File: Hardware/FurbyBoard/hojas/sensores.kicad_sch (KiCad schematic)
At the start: 39 parts, among them J10 Luz ×2, altavoz ×2, J7 IR: emisor ×2, receptor ×3, G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, J8 Inclinación ×3, lengua ×2, J9 Leva ×2, encoder ×4, barriga 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, Q2 AO3400A, Q3 AO3400A, U10 TCA9535PWR, U11 SN74LVC1G17DBVR

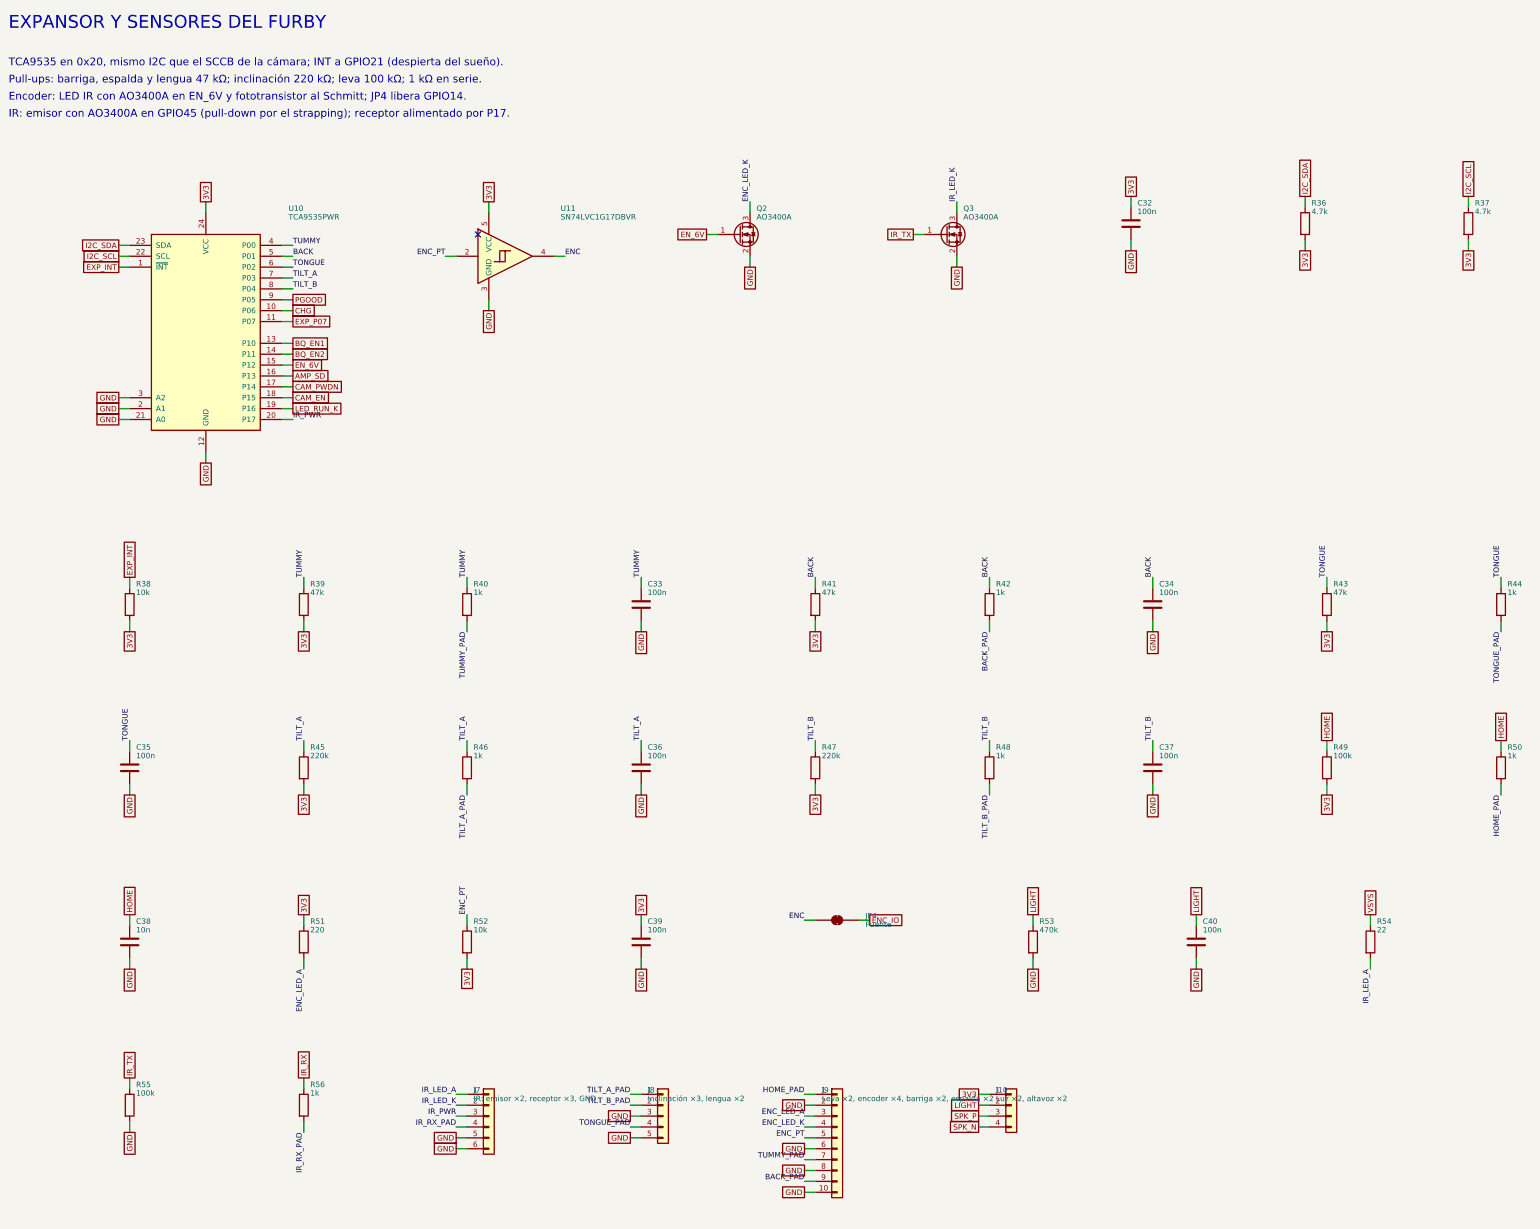
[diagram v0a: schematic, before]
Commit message: Refactor: pads de cable agrupados por zona y etiquetas globales
- Motor en J9 con leva, encoder y sensores; altavoz en J8 con inclinación y
  lengua; luz en J7 con el IR. Desaparecen J4 y J10: cada grupo sale por el
  borde más cercano a su destino.
- Micro en 2x03 en vez de 1x06 para que quepa junto al borde derecho.
- Todas las etiquetas del esquemático son globales, así el nombre de red
  coincide con el del PCB (paridad sin prefijos de hoja).
- ERC 0 errores, 0 avisos.

Co-Authored-By: Claude Opus 5.5 (1M context) <noreply@anthropic.com>
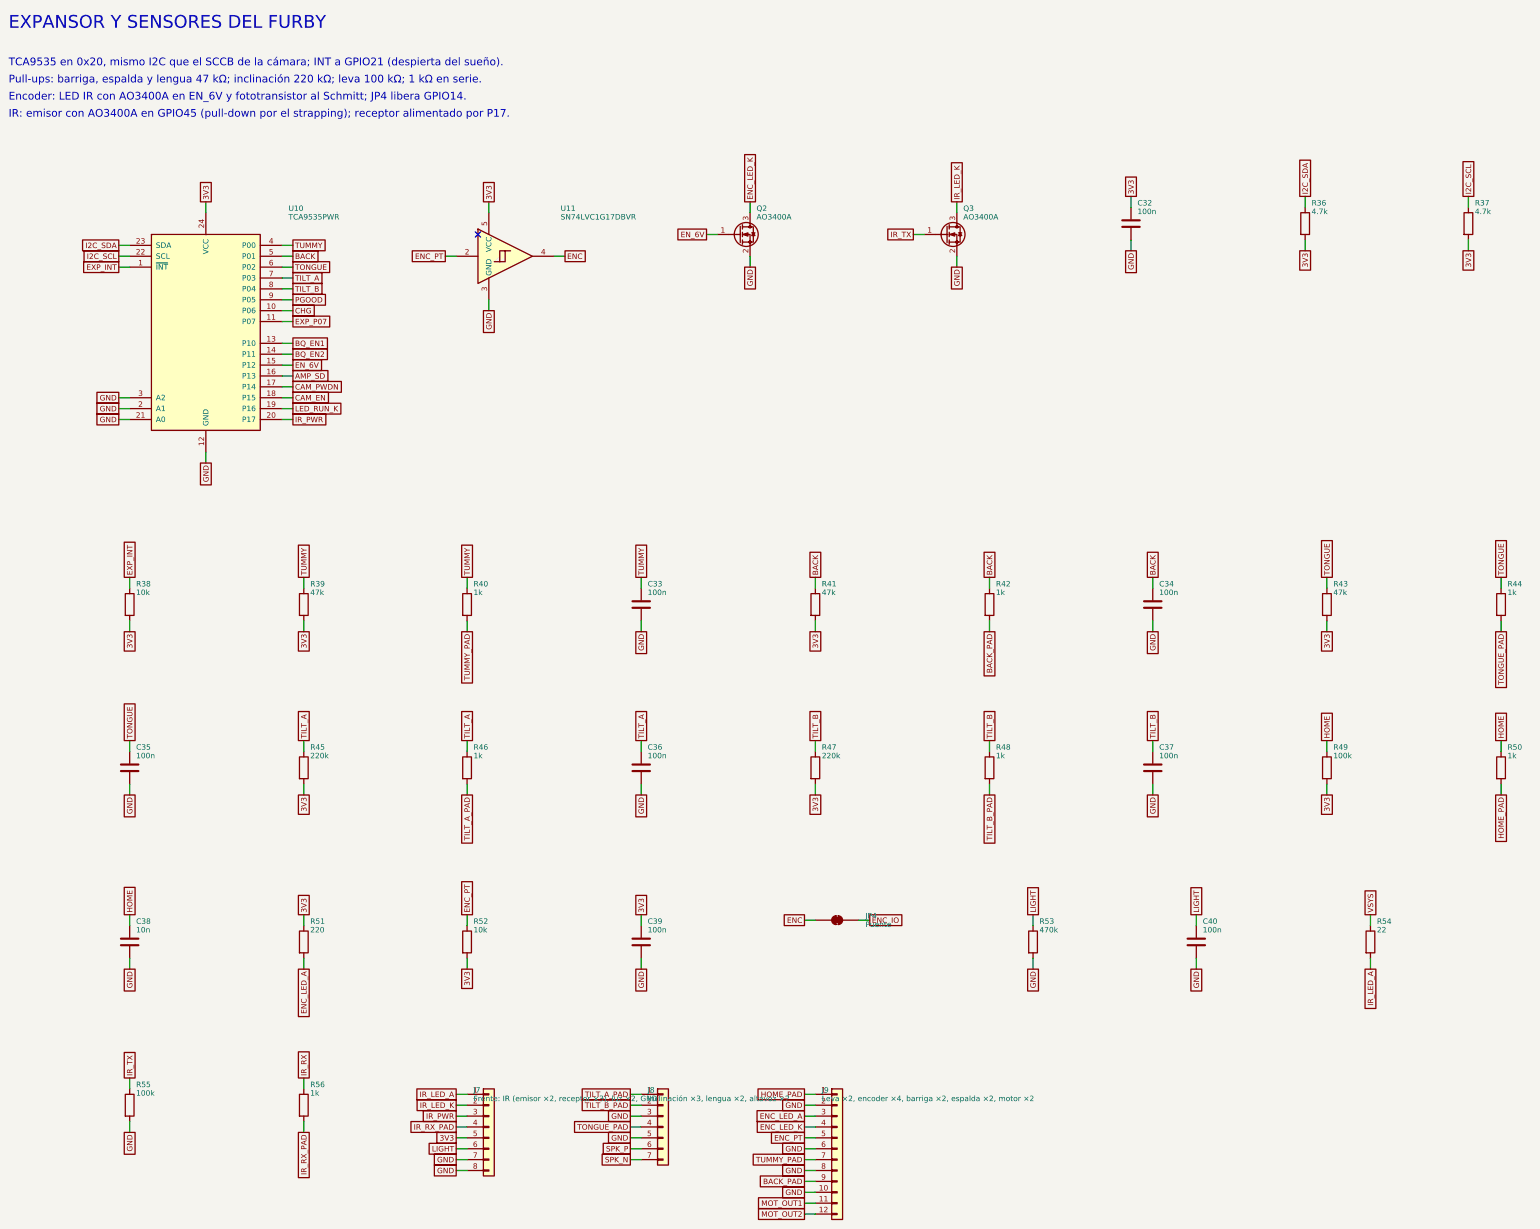
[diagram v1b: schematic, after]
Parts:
- removed J10: Luz ×2, altavoz ×2, FurbyBoard:Pads_2x02_P2.54mm, symbol Connector_Generic:Conn_01x04
- J7: value IR: emisor ×2, receptor ×3, GND -> Frente: IR (emisor ×2, receptor ×3), luz ×2, GND; footprint FurbyBoard:Pads_2x03_P2.54mm -> FurbyBoard:Pads_2x04_P2.54mm; symbol Connector_Generic:Conn_01x06 -> Connector_Generic:Conn_01x08
- J8: value Inclinación ×3, lengua ×2 -> Inclinación ×3, lengua ×2, altavoz ×2; footprint FurbyBoard:Pads_1x05_P2.54mm -> FurbyBoard:Pads_1x07_P2.54mm; symbol Connector_Generic:Conn_01x05 -> Connector_Generic:Conn_01x07
- J9: value Leva ×2, encoder ×4, barriga ×2, espalda ×2 -> Leva ×2, encoder ×4, barriga ×2, espalda ×2, motor ×2; footprint FurbyBoard:Pads_2x05_P2.54mm -> FurbyBoard:Pads_2x06_P2.54mm; symbol Connector_Generic:Conn_01x10 -> Connector_Generic:Conn_01x12
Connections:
- net 3V3: now also J7.5 (Pin_5)
- net GND: now also J7.7 (Pin_7), J7.8 (Pin_8); no longer J7.5 (Pin_5), J7.6 (Pin_6)
- net LIGHT: now also J7.6 (Pin_6)
- net SPK_N: now also J8.7 (Pin_7)
- net SPK_P: now also J8.6 (Pin_6)
- new net MOT_OUT1: J9.11 (Pin_11)
- new net MOT_OUT2: J9.12 (Pin_12)

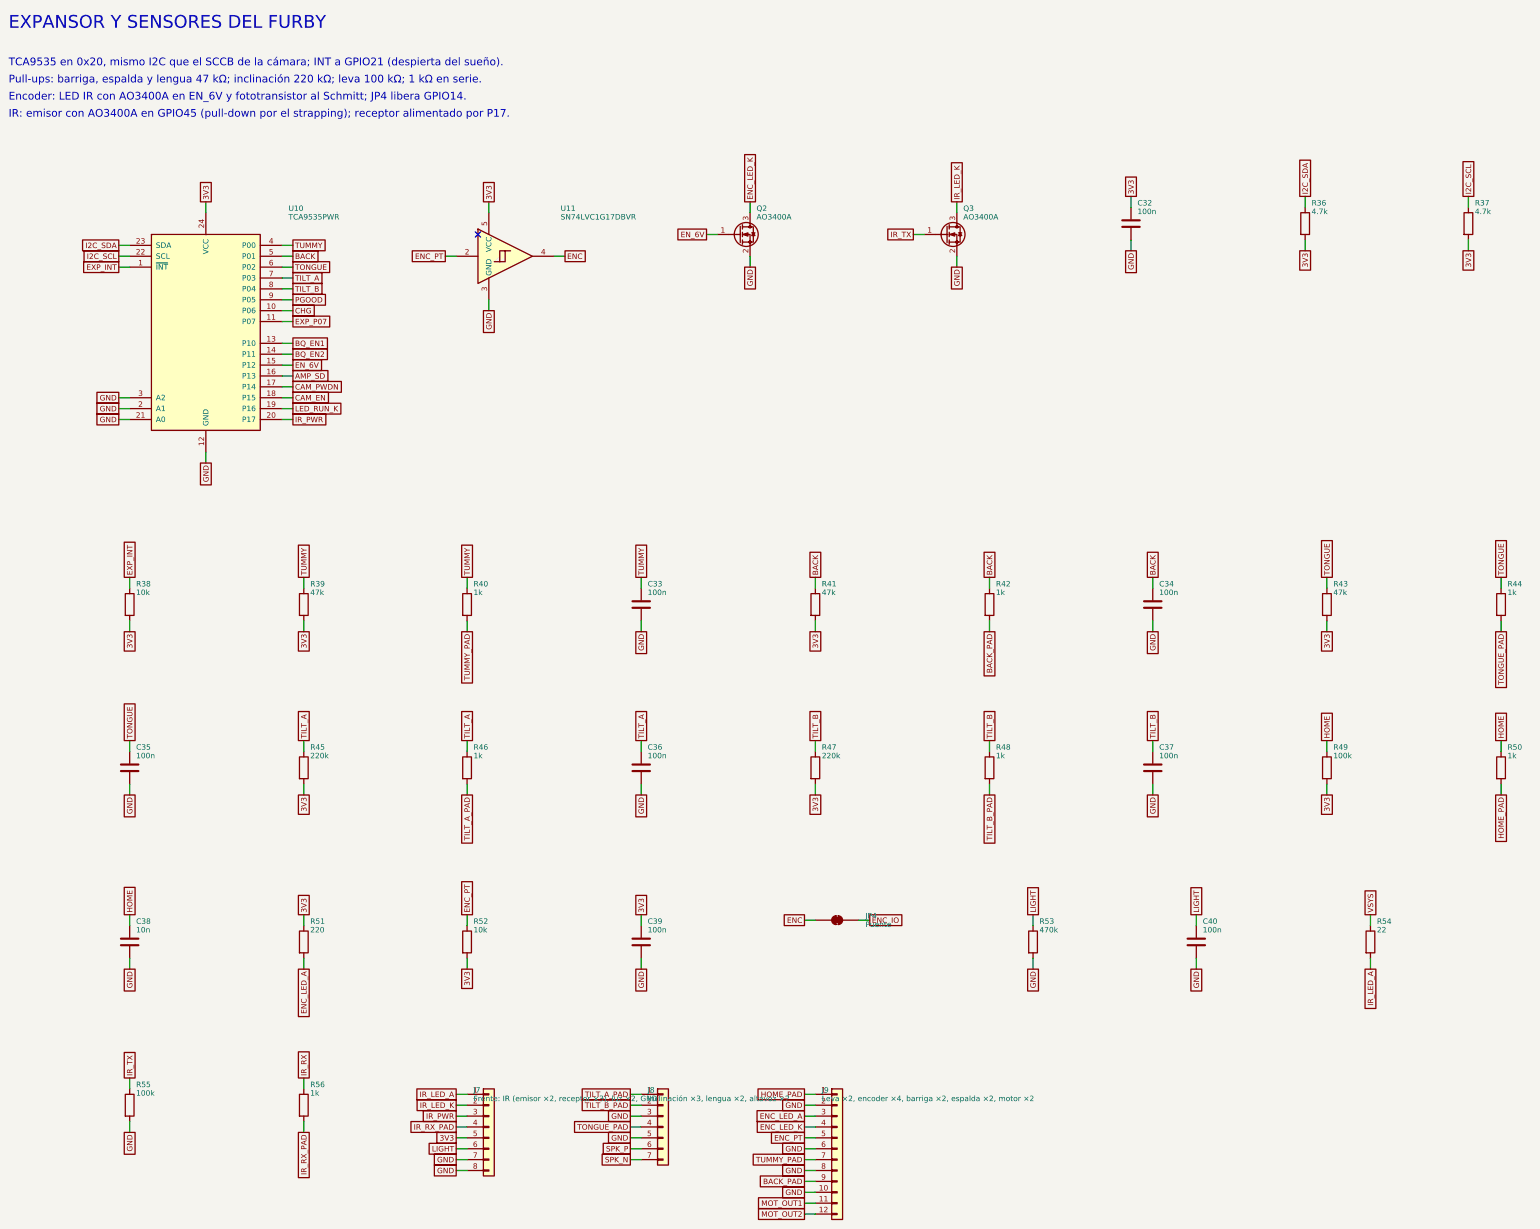
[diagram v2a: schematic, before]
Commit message: Feature: esquema de la FurbyBoard al procedimiento nuevo: rúbrica L, reglas por red, pines por geometría y simulación del elevador
- Rúbrica S/M/L (L) y tabla de raíles con anchos mínimos (params.ANCHOS_MINIMOS), que gen_pro.py vuelca al .kicad_dru como una regla por red, con cuellos dentro de los patios de los QFN y de J1.
- Vías de 0,45/0,2 solo en la clase USB (cruce del par en el receptáculo de 16 pines); el resto sigue en 0,6/0,3.
- pcb-toolkit.toml: clases B/C/D, anchos, grupos explícitos y zonas del puente H y de la clase D.
- Redes a la convención: BB_SW1/2, I2S_SCK_MIC/I2S_WS_MIC.
- Pines del módulo (I2S, HOME, EXP_INT) y puertos del TCA9535 por geometría, sin tocar strapping, USB ni ADC.
- LED del encoder desde V6 por 470 ohm (sin Q2); J_EXP 2x5; J9 y J5 reordenados; serigrafía al día.
- ERC 0/0. Simulación ngspice del elevador en el peor caso (sim/). Informes de las puertas A y B en revisiones/; un crítico (NTC del cargador) queda escalado.

Co-Authored-By: Claude Fable 5.1 <noreply@anthropic.com>
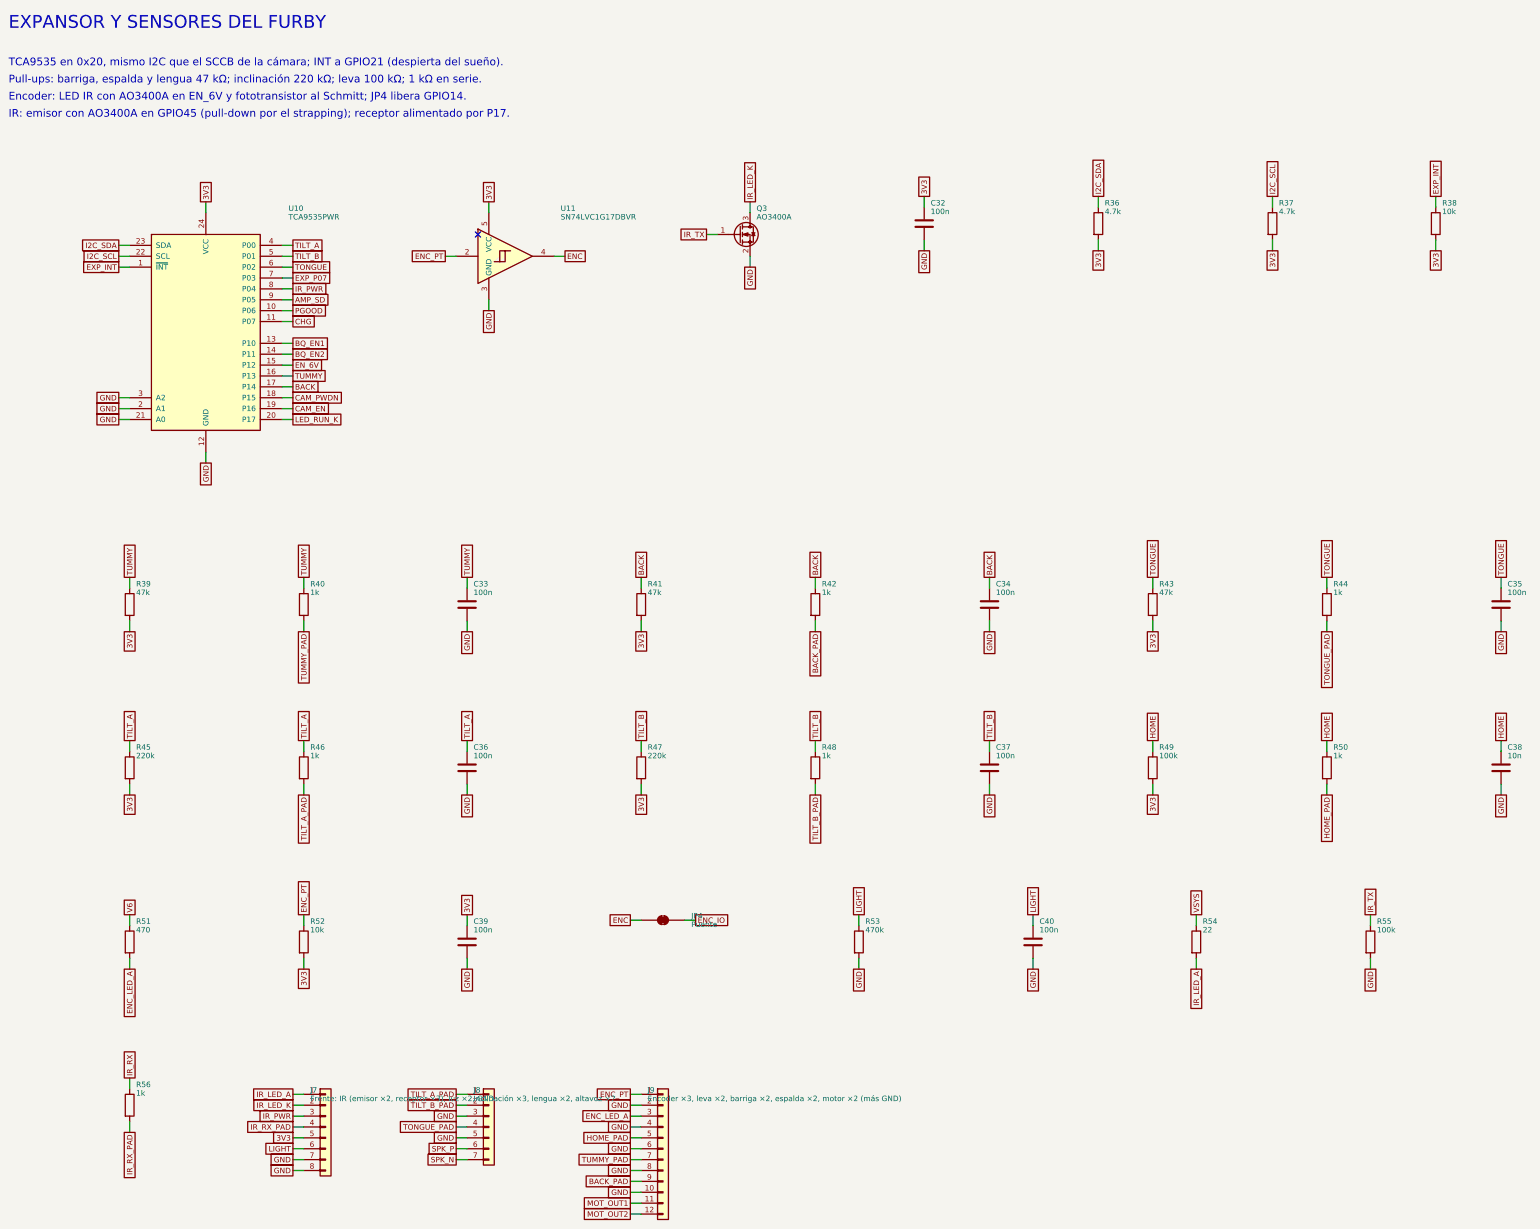
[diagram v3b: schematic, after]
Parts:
- removed Q2: AO3400A, Package_TO_SOT_SMD:SOT-23, symbol Transistor_FET:Q_NMOS_GSD
- J9: value Leva ×2, encoder ×4, barriga ×2, espalda ×2, motor ×2 -> Encoder ×3, leva ×2, barriga ×2, espalda ×2, motor ×2 (más GND)
- R51: value 220 -> 470; LCSC C22962 -> C23179
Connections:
- net ENC_LED_K is gone; now on net GND: J9.4 (Pin_4)
- net 3V3: no longer R51.1
- net AMP_SD: now also U10.9 (P05); no longer U10.16 (P13)
- net BACK: now also U10.17 (P14); no longer U10.5 (P01)
- net CAM_EN: now also U10.19 (P16); no longer U10.18 (P15)
- net CAM_PWDN: now also U10.18 (P15); no longer U10.17 (P14)
- net CHG: now also U10.11 (P07); no longer U10.10 (P06)
- net ENC_PT: now also J9.1 (Pin_1); no longer J9.5 (Pin_5)
- net EXP_P07: now also U10.7 (P03); no longer U10.11 (P07)
- net HOME_PAD: now also J9.5 (Pin_5); no longer J9.1 (Pin_1)
- net IR_PWR: now also U10.8 (P04); no longer U10.20 (P17)
- net LED_RUN_K: now also U10.20 (P17); no longer U10.19 (P16)
- net PGOOD: now also U10.10 (P06); no longer U10.9 (P05)
- net TILT_A: now also U10.4 (P00); no longer U10.7 (P03)
- net TILT_B: now also U10.5 (P01); no longer U10.8 (P04)
- net TUMMY: now also U10.16 (P13); no longer U10.4 (P00)
- new net V6: R51.1
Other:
- moved on the sheet: C32, C33, C34, C35, C36, C37, C38, C39, C40, J7, J8, J9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

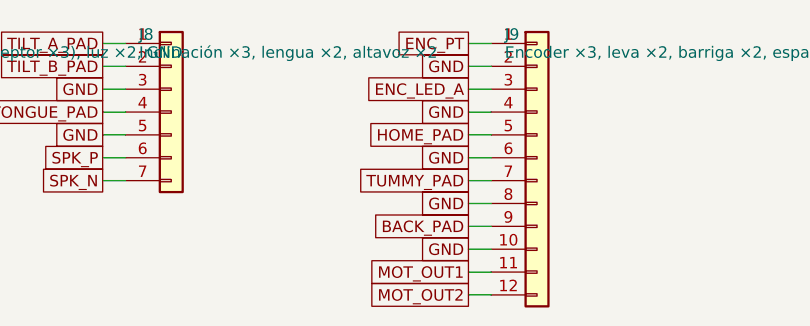
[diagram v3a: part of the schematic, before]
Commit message: Feature: rutado del puente H, el amplificador y las vías de VSYS/GND de potencia
U6: V6 a C21/C19/C22/C20 y al pin 5, OUT2 a J9.11 por F.Cu y OUT1 a J9.12 por In2
(pads 11/12 del motor intercambiados en el esquema; ERC 0), IPROPI a R28/TP8 y por In2 a
JP3 fuera del anillo del mecanismo, VREF a C23/R27/R26, EP con 2 vías. U7: VSYS a C26 y
vías, GND al EP, SPK_P/N a J8 en diagonales separadas. Vías de VSYS de L2, R54, R6, C24,
C25 y C17; vías de GND de los pasivos de los dos bloques. Puerta D: DRC 0/0, revisar-rutado
0 errores (48 avisos documentados), PNG de U6, U7 y B.Cu de U6 revisados.

Co-Authored-By: Claude Fable 5.1 <noreply@anthropic.com>
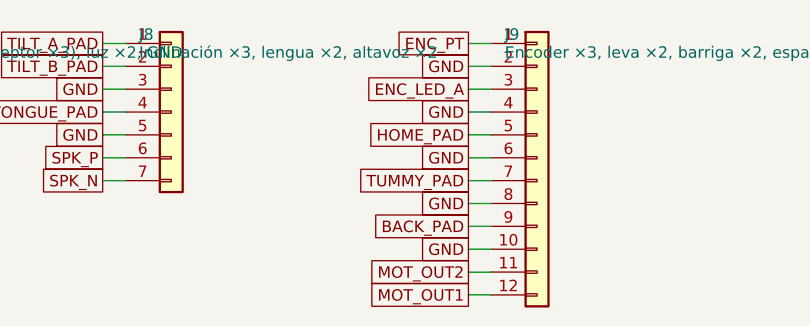
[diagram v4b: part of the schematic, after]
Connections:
- net MOT_OUT1: now also J9.12 (Pin_12); no longer J9.11 (Pin_11)
- net MOT_OUT2: now also J9.11 (Pin_11); no longer J9.12 (Pin_12)
